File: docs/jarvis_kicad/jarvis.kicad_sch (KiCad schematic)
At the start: 4 parts, among them SW1 Down Tactile Button, SW2 Up Tactile Button, U1 ESP32-WROOM-32

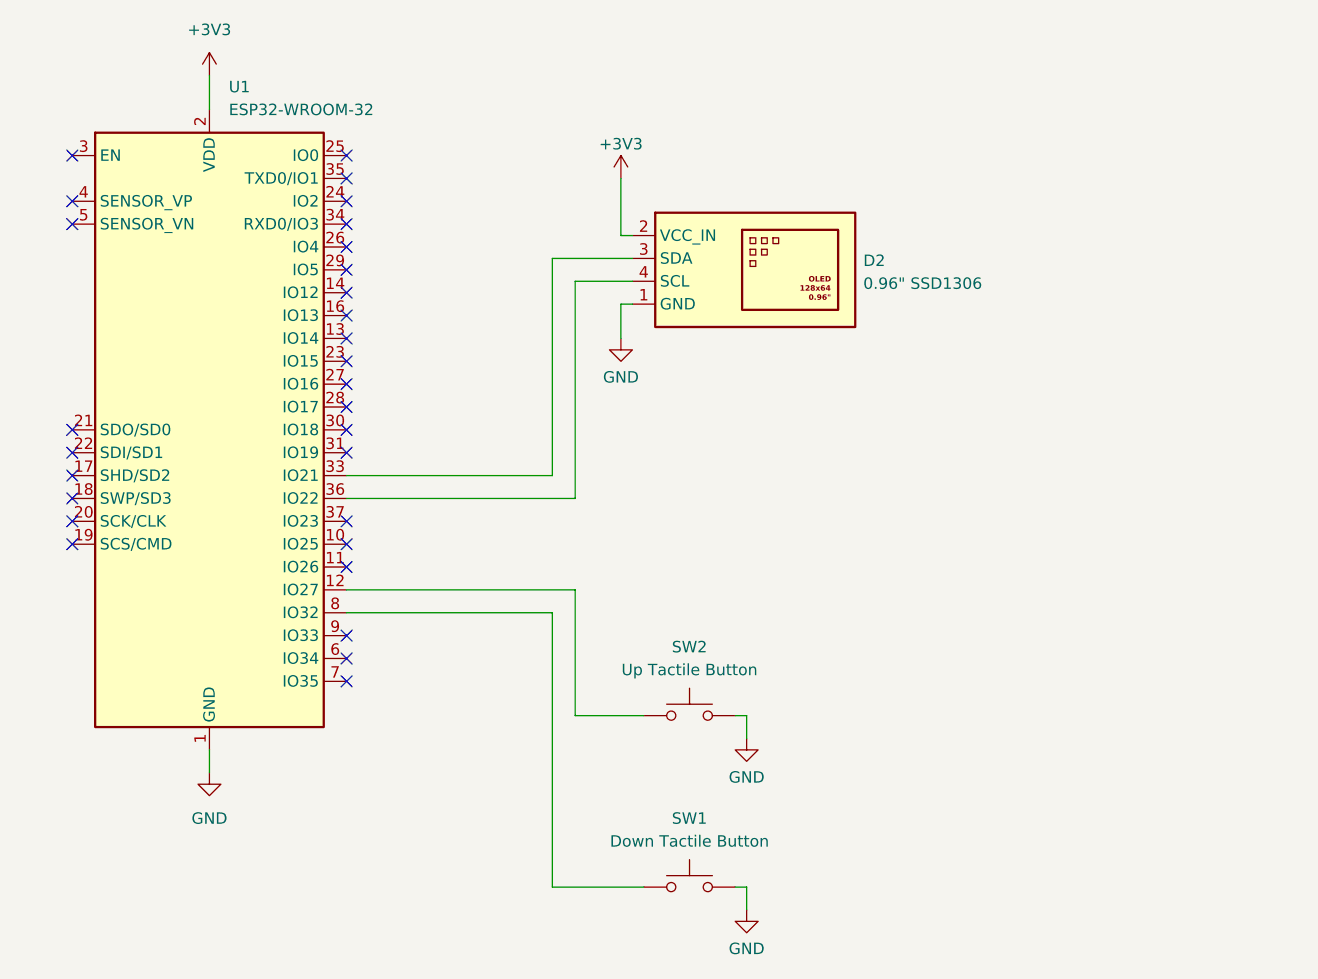
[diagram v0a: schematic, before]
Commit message: feat(hardware): migrate to ESP32-C6 and remap pins * Switch the PlatformIO platform and board to the ESP32-C6 and update the GPIO assignments to match the new board's pinout. * Buttons move to GPIO4 (up) and GPIO5 (down) * OLED display moves to GPIO19 (SDA) and GPIO20 (SCL) * Update WiFi status call for the C6 core API
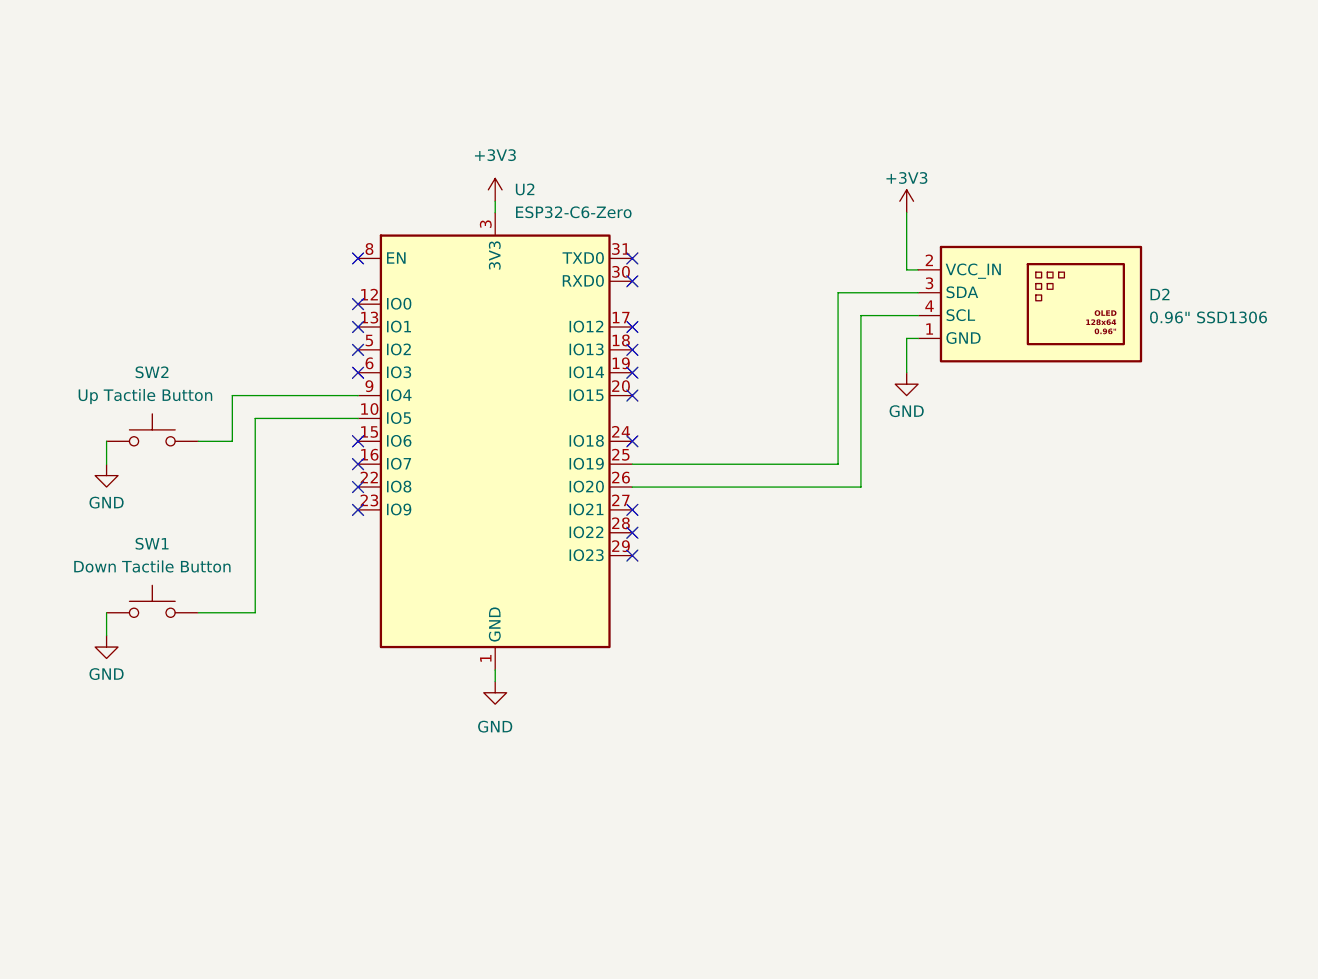
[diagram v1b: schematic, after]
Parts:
- removed U1: ESP32-WROOM-32, RF_Module:ESP32-WROOM-32, symbol RF_Module:ESP32-WROOM-32
- added U2: ESP32-C6-Zero, RF_Module:ESP32-C6-MINI-1, symbol RF_Module:ESP32-C6-MINI-1
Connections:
- net +3V3: now also U2.3 (3V3)
- net GND: now also SW1.1, SW2.1, U2.1 (GND), U2.11 (GND), U2.14 (GND), U2.2 (GND), U2.36 (GND), U2.37 (GND), U2.38 (GND), U2.39 (GND), U2.40 (GND), U2.41 (GND), U2.42 (GND), U2.43 (GND), U2.44 (GND), U2.45 (GND), U2.46 (GND), U2.47 (GND), U2.48 (GND), U2.49 (GND), U2.50 (GND), U2.51 (GND), U2.52 (GND), U2.53 (GND); no longer SW1.2, SW2.2
- net at D2.3 (SDA): now also U2.25 (IO19)
- net at D2.4 (SCL): now also U2.26 (IO20)
- new net: SW1.2, U2.10 (IO5)
- new net: SW2.2, U2.9 (IO4)
- no-connect marks 29 -> 19
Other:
- moved on the sheet: D2, SW1, SW2

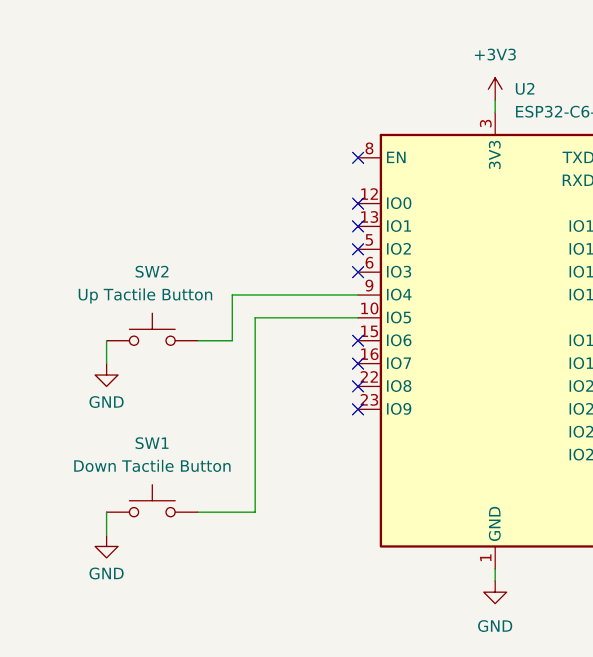
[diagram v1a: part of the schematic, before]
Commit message: refactor(input): replace button handling with a new Input class and remove deprecated button files (now using touch sensor)
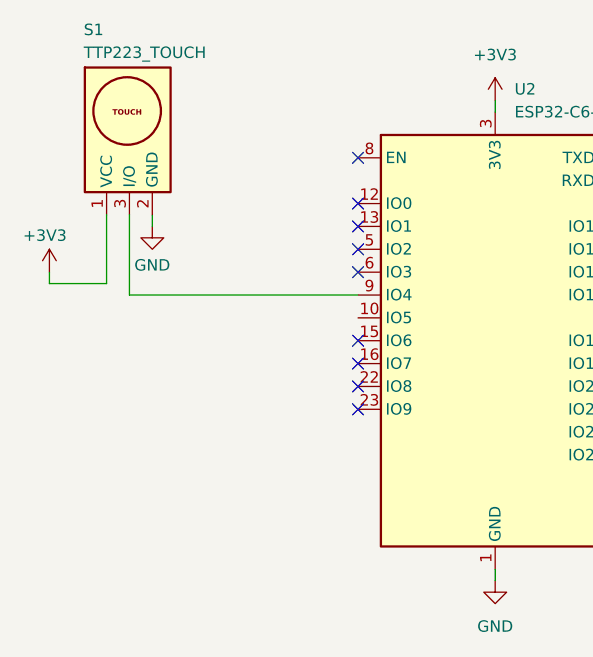
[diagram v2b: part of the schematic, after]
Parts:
- removed SW1: Down Tactile Button, Button_Switch_THT:SW_PUSH_6mm, symbol Switch:SW_Push
- removed SW2: Up Tactile Button, Button_Switch_THT:SW_PUSH_6mm, symbol Switch:SW_Push
- added S1: TTP223_TOUCH, symbol arduino:TTP223_TOUCH
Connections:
- net +3V3: now also S1.1 (VCC)
- net GND: now also S1.2 (GND)
- net at U2.9 (IO4): now also S1.3 (I/O)
